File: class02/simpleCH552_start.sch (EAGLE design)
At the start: 6 parts, among them U1 CH552G, X1 USBPCB

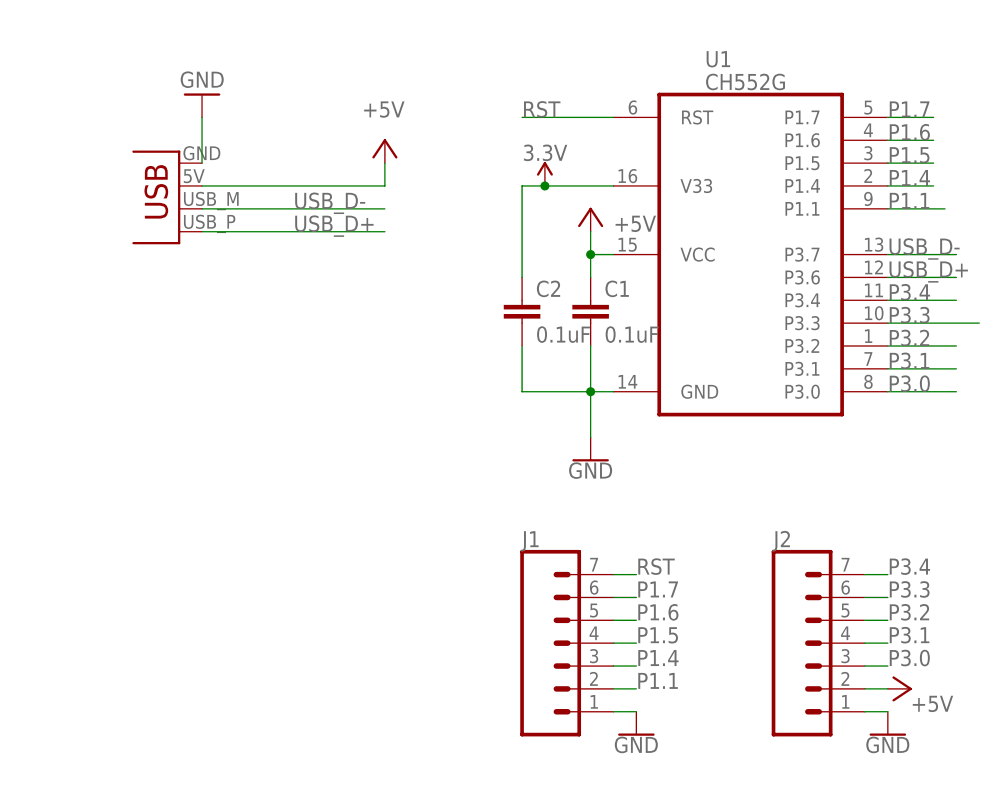
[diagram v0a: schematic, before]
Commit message: update to USB shell model
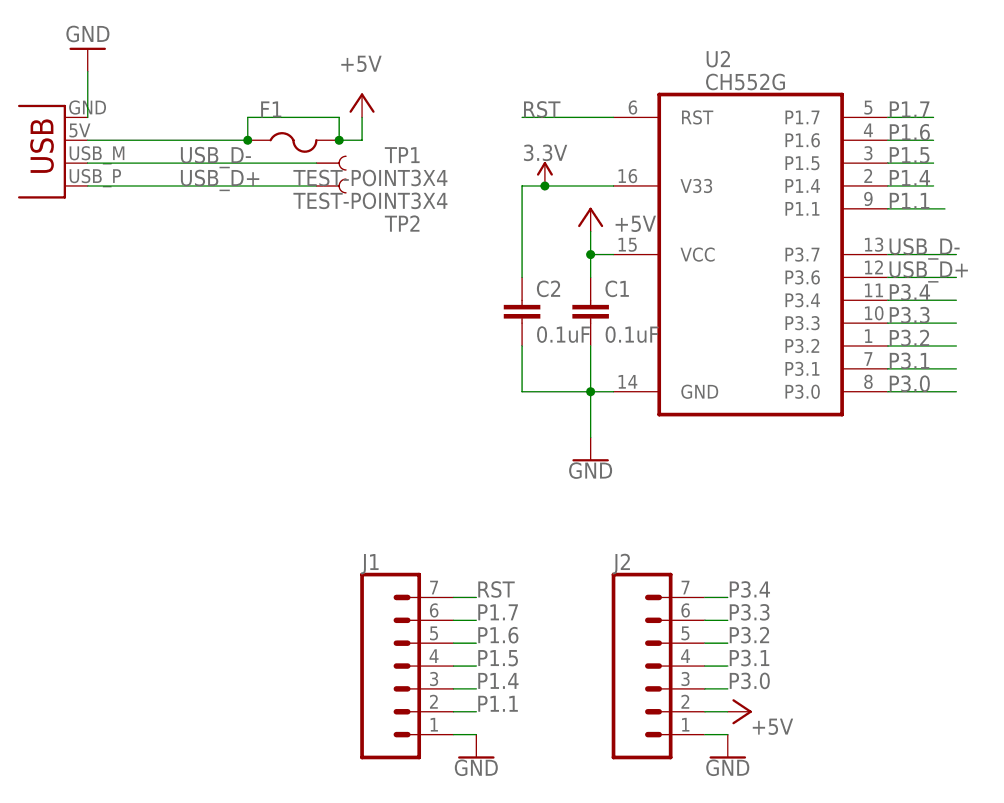
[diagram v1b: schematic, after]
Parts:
- added F1: (no value), adafruit:PTCFUSE-1206
- added TP1, TP2: TEST-POINT3X4, SparkFun-Connectors:TEST-POINT3X4
- renumbered U1 to U2
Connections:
- net +5V: now also F1.1, F1.2
- net USB_D+: now also TP2.1
- net USB_D-: now also TP1.1
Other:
- moved on the sheet: J1, J2
